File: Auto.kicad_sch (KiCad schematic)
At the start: 25 parts, among them J10 M2, J11 M3, J12 M4, J5 HC-SR04, J9 M1, U4 74HC595, U5 L293DD, U6 L293DD

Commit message: Finalizo el esquematico
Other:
- note added: "OE 0: Habilita enables de drivers y salida de registro de desplazamiento, inhabilita salidas a servos 1: Habilita salidas a servos, inhabilita enables de drivers y salida de registro de desplazamiento"
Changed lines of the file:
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@@
+		)
+	)
+	(text "OE\n0: Habilita enables de drivers y salida de registro de desplazamiento, inhabilita salidas a servos\n1: Habilita salidas a servos, inhabilita enables de drivers y salida de registro de desplazamiento"
+		(exclude_from_sim no)
+		(at 52.832 106.172 0)
+		(effects
+			(font
+				(size 1.27 1.27)
+			)
 		)
 	)

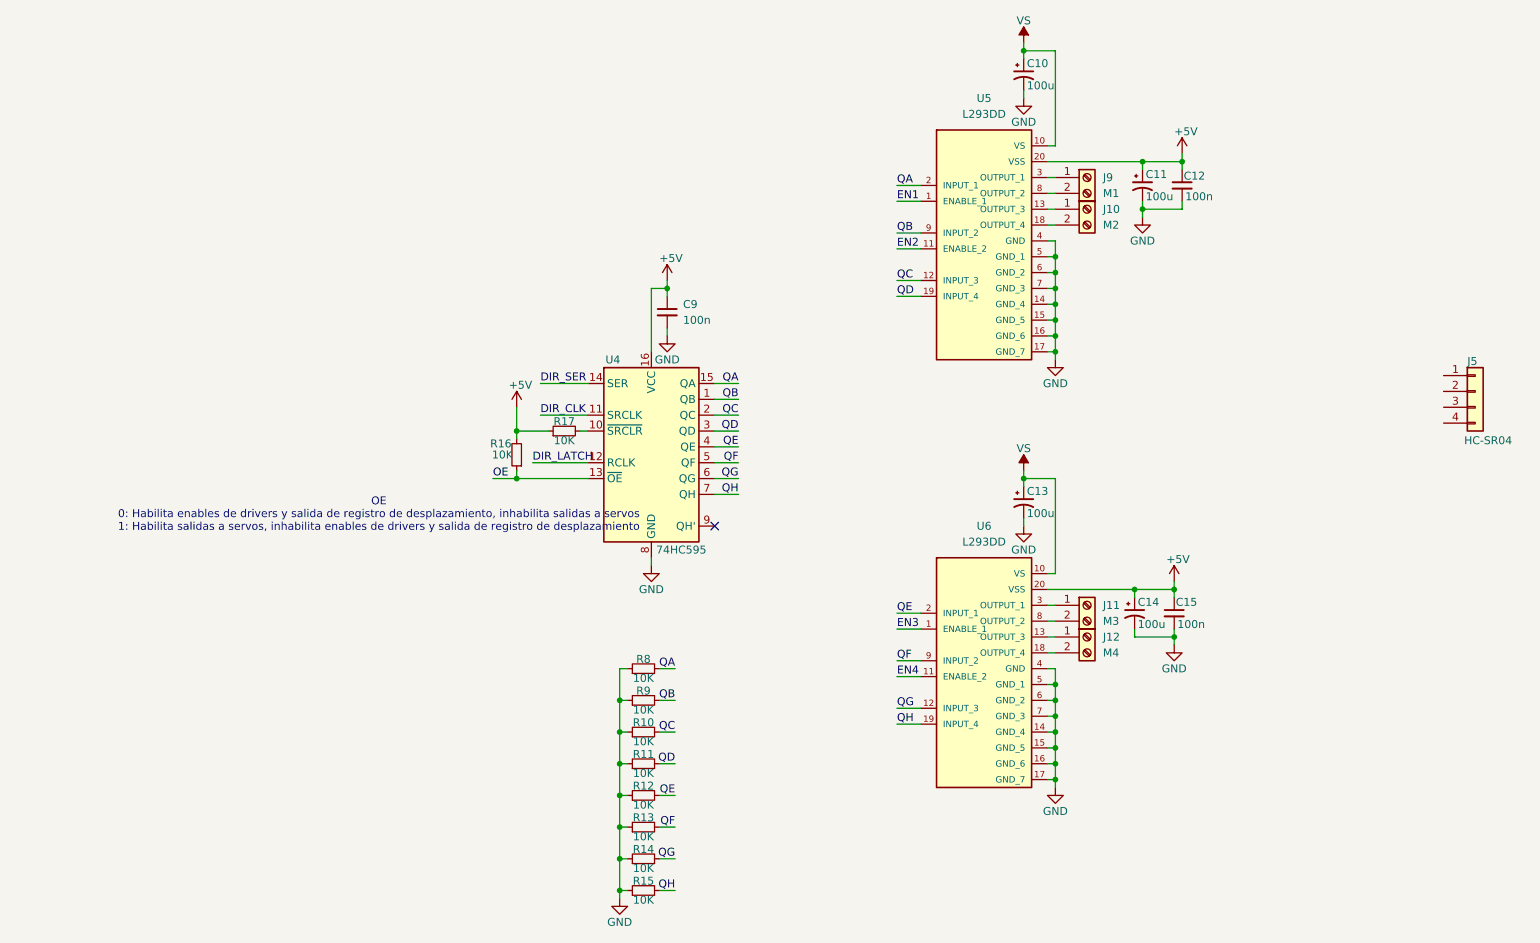
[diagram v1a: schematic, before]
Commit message: Reseteo numeracion de componentes
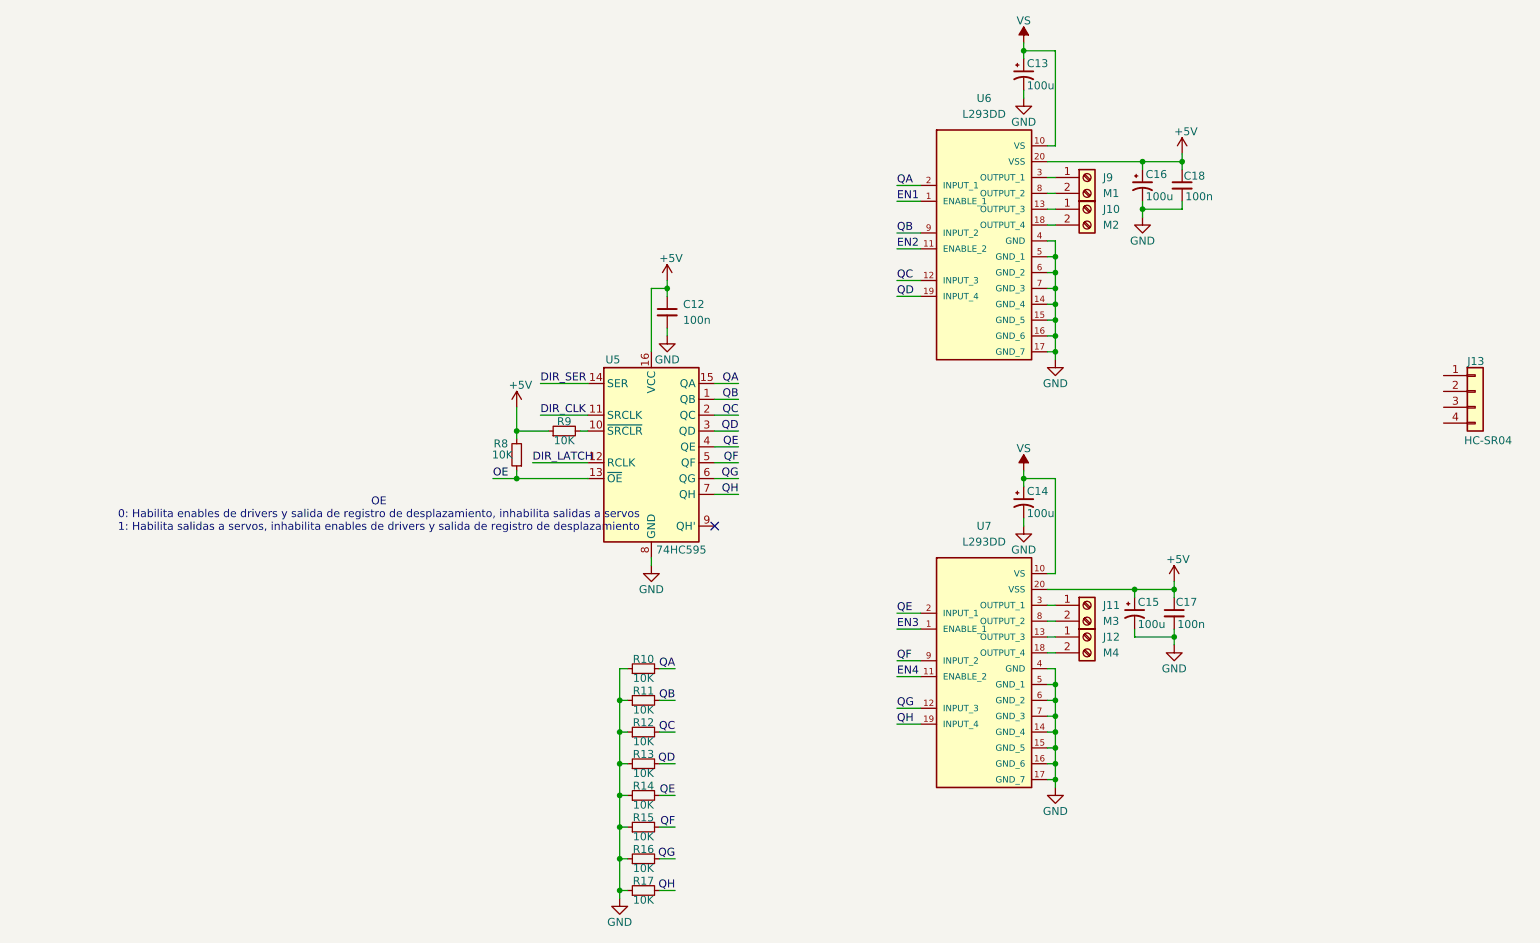
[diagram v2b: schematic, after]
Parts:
- renumbered C9 to C12, C10 to C13, C13 to C14, C14 to C15, C11 to C16, C15 to C17, C12 to C18, J5 to J13, R8 to R10, R9 to R11, R10 to R12, R11 to R13, R12 to R14, R13 to R15, R14 to R16, R15 to R17, R16 to R8, R17 to R9, U4 to U5, U5 to U6, U6 to U7

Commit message: Termino lista de materiales, ubico componentes e inicio ruteo
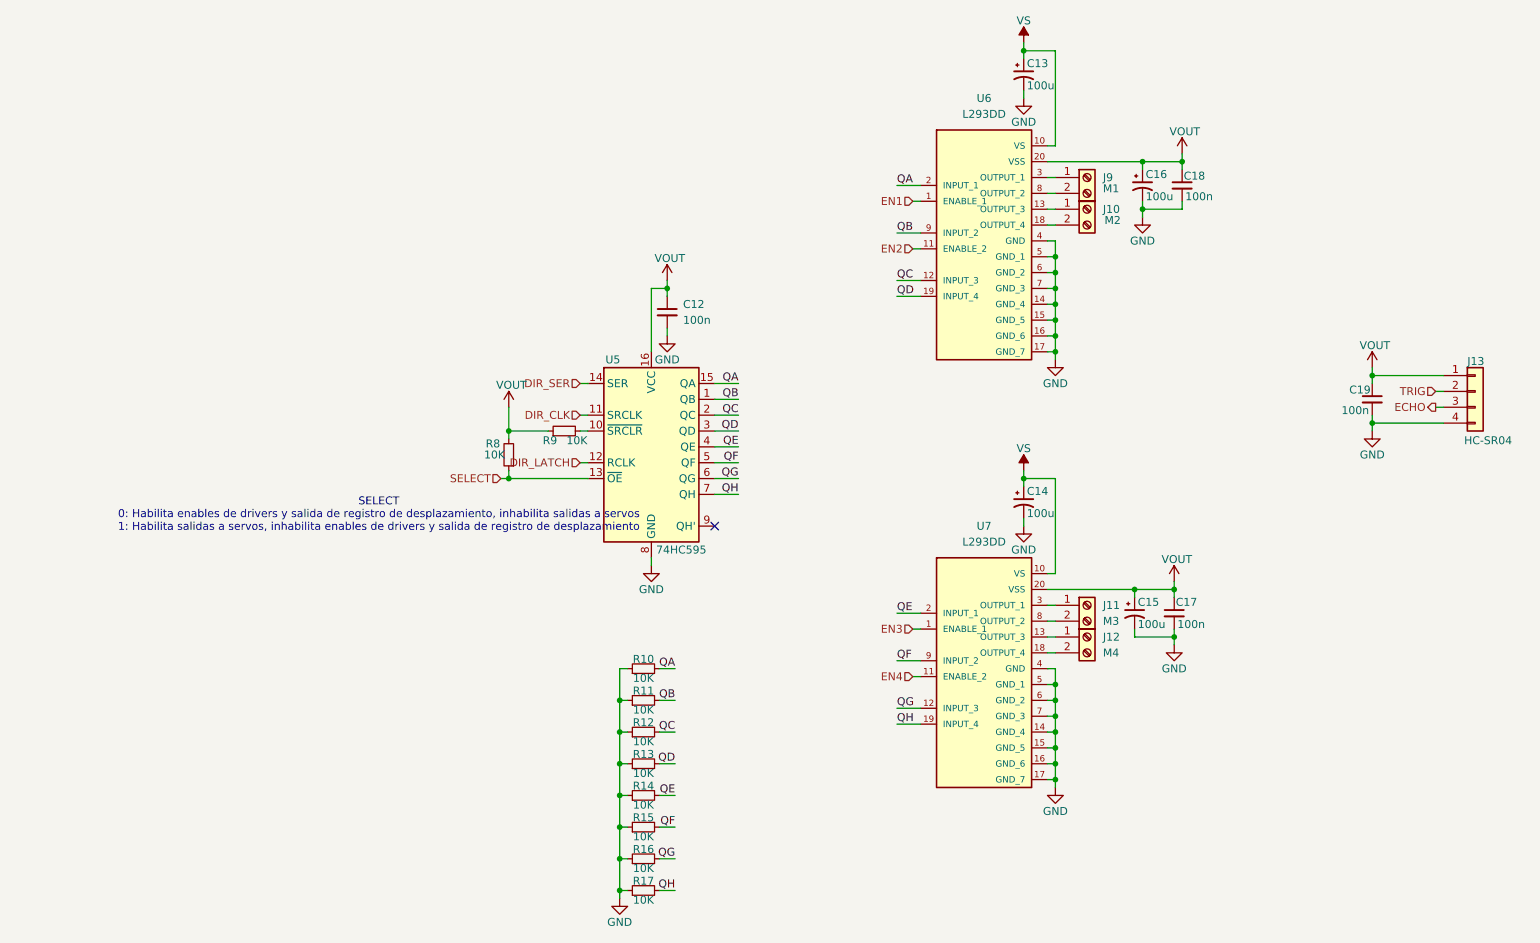
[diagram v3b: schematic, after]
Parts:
- added C19: 100n, Capacitor_SMD:C_0603_1608Metric_Pad1.08x0.95mm_HandSolder, symbol Device:C_Small
- C12, C17, C18: PartNumber (none) -> CL10B104KB8NNNC; PurchaseLink (none) -> https://www.digikey.com/short/0f3djmh4
- C13, C14, C15, C16: footprint Newsanlib:CAP_EEEFK1E101XP -> Capacitor_SMD:CP_Elec_6.3x5.9; PartNumber (none) -> A765EB107M1CLAE025; PurchaseLink (none) -> https://www.digikey.com/en/products/detail/kemet/A765EB107M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
- J13: footprint Connector_PinHeader_1.27mm:PinHeader_1x04_P1.27mm_Vertical -> Connector_PinHeader_2.54mm:PinHeader_1x04_P2.54mm_Vertical
- R10, R11, R12, R13, R14, R15, R16, R17, R8, R9: PartNumber (none) -> RC0603FR-0710KL; PurchaseLink (none) -> https://www.digikey.com/en/products/detail/yageo/RC0603FR-0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
- U5: footprint Package_SO:SOIC-16W_5.3x10.2mm_P1.27mm -> Package_SO:TSSOP-16_4.4x5mm_P0.65mm; PartNumber (none) -> 74HC595PW-Q100,118; PurchaseLink (none) -> https://www.digikey.com/en/products/detail/nexperia-usa-inc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
- U6, U7: PurchaseLink (none) -> https://www.digikey.com/en/products/detail/stmicroelectroni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
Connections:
- net +5V is gone; now on net VOUT: C12.1, C15.1, C16.1, C17.1, C18.1, R8.2, R9.1, U5.16 (VCC), U6.20 (VSS), U7.20 (VSS)
- net GND: now also J13.4 (Pin_4), C19.2
- net VOUT: now reaches J13.1 (Pin_1)
- net VOUT: now also C19.1
- net TRIG: now reaches J13.2 (Pin_2)
- net ECHO: now reaches J13.3 (Pin_3)
- net OE renamed SELECT
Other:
- note added: "SELECT 0: Habilita enables de drivers y salida de registro de desplazamiento, inhabilita salidas a servos 1: Habilita salidas a servos, inhabilita enables de drivers y salida de registro de desplazamiento"
- note removed: "OE 0: Habilita enables de drivers y salida de registro de desplazamiento, inhabilita salidas a servos 1: Habilita salidas a servos, inhabilita enables de drivers y salida de registro de desplazamiento"
- moved on the sheet: R8

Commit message: Agrego capacitores y cambio footprints de borneras
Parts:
- J10, J11, J12, J9: footprint Newsanlib:TerminalBlock_bornier-2_P5.08mm -> TerminalBlock_RND:TerminalBlock_RND_205-00287_1x02_P5.08mm_Horizontal
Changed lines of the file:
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@@
 			)
 		)
-		(property "Footprint" "Newsanlib:TerminalBlock_bornier-2_P5.08mm"
+		(property "Footprint" "TerminalBlock_RND:TerminalBlock_RND_205-00287_1x02_P5.08mm_Horizontal"
 			(at 166.37 120.65 0)
 			(effects
@@
 			)
 		)
-		(property "Footprint" "Newsanlib:TerminalBlock_bornier-2_P5.08mm"
+		(property "Footprint" "TerminalBlock_RND:TerminalBlock_RND_205-00287_1x02_P5.08mm_Horizontal"
 			(at 166.37 52.07 0)
 			(effects
@@
 			)
 		)
-		(property "Footprint" "Newsanlib:TerminalBlock_bornier-2_P5.08mm"
+		(property "Footprint" "TerminalBlock_RND:TerminalBlock_RND_205-00287_1x02_P5.08mm_Horizontal"
 			(at 166.37 125.73 0)
 			(effects
@@
 			)
 		)
-		(property "Footprint" "Newsanlib:TerminalBlock_bornier-2_P5.08mm"
+		(property "Footprint" "TerminalBlock_RND:TerminalBlock_RND_205-00287_1x02_P5.08mm_Horizontal"
 			(at 166.37 57.15 0)
 			(effects

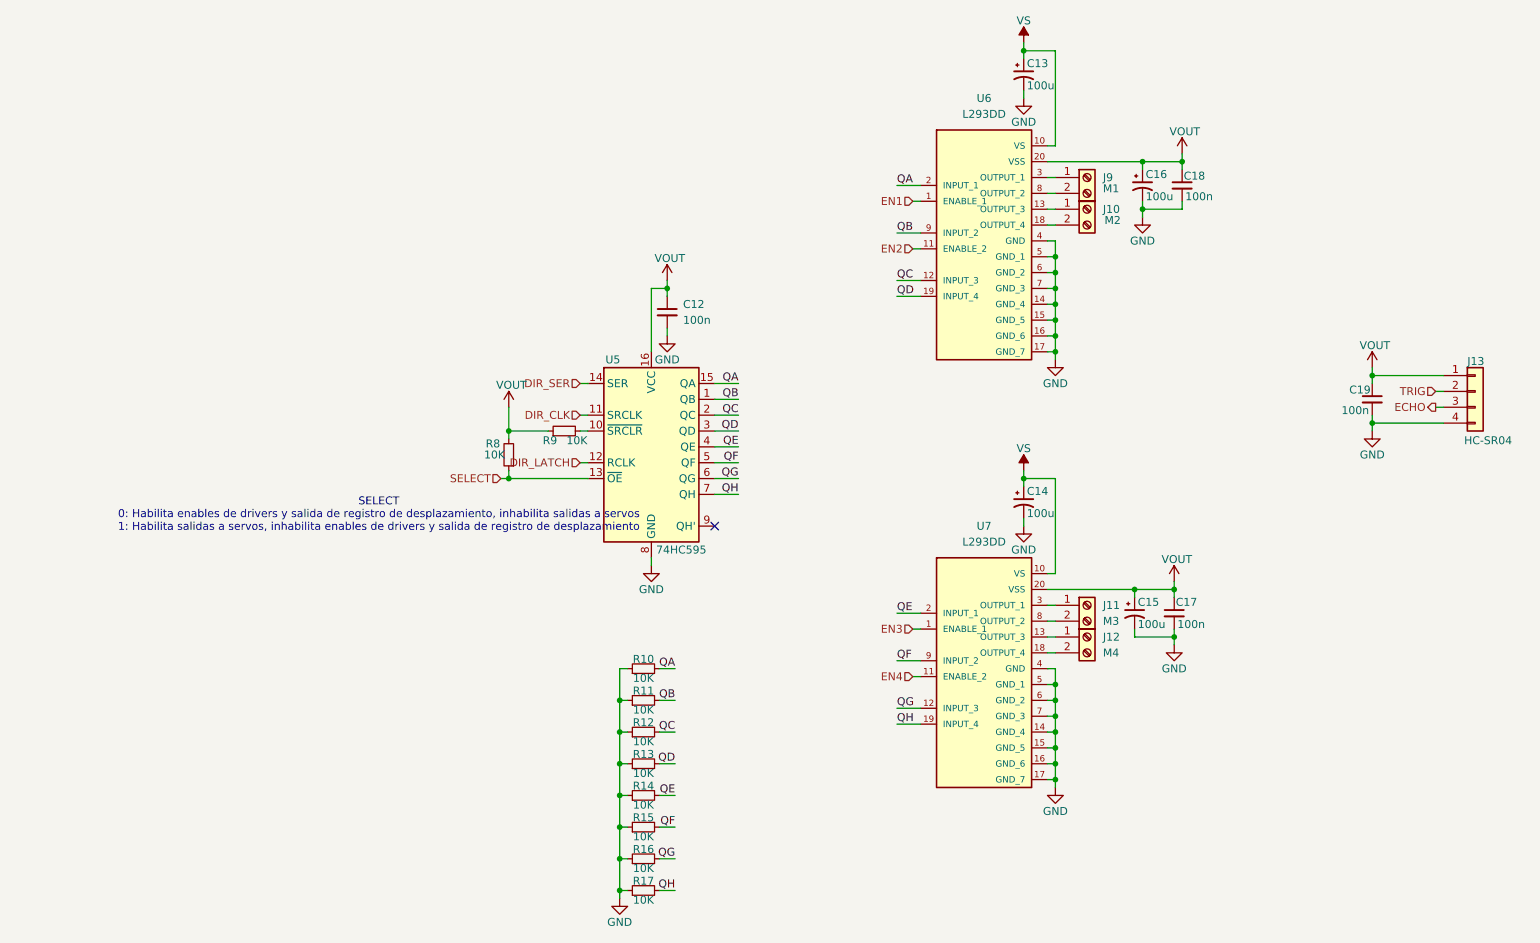
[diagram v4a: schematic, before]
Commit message: Cambio componente principal, hago ubicación en PCB
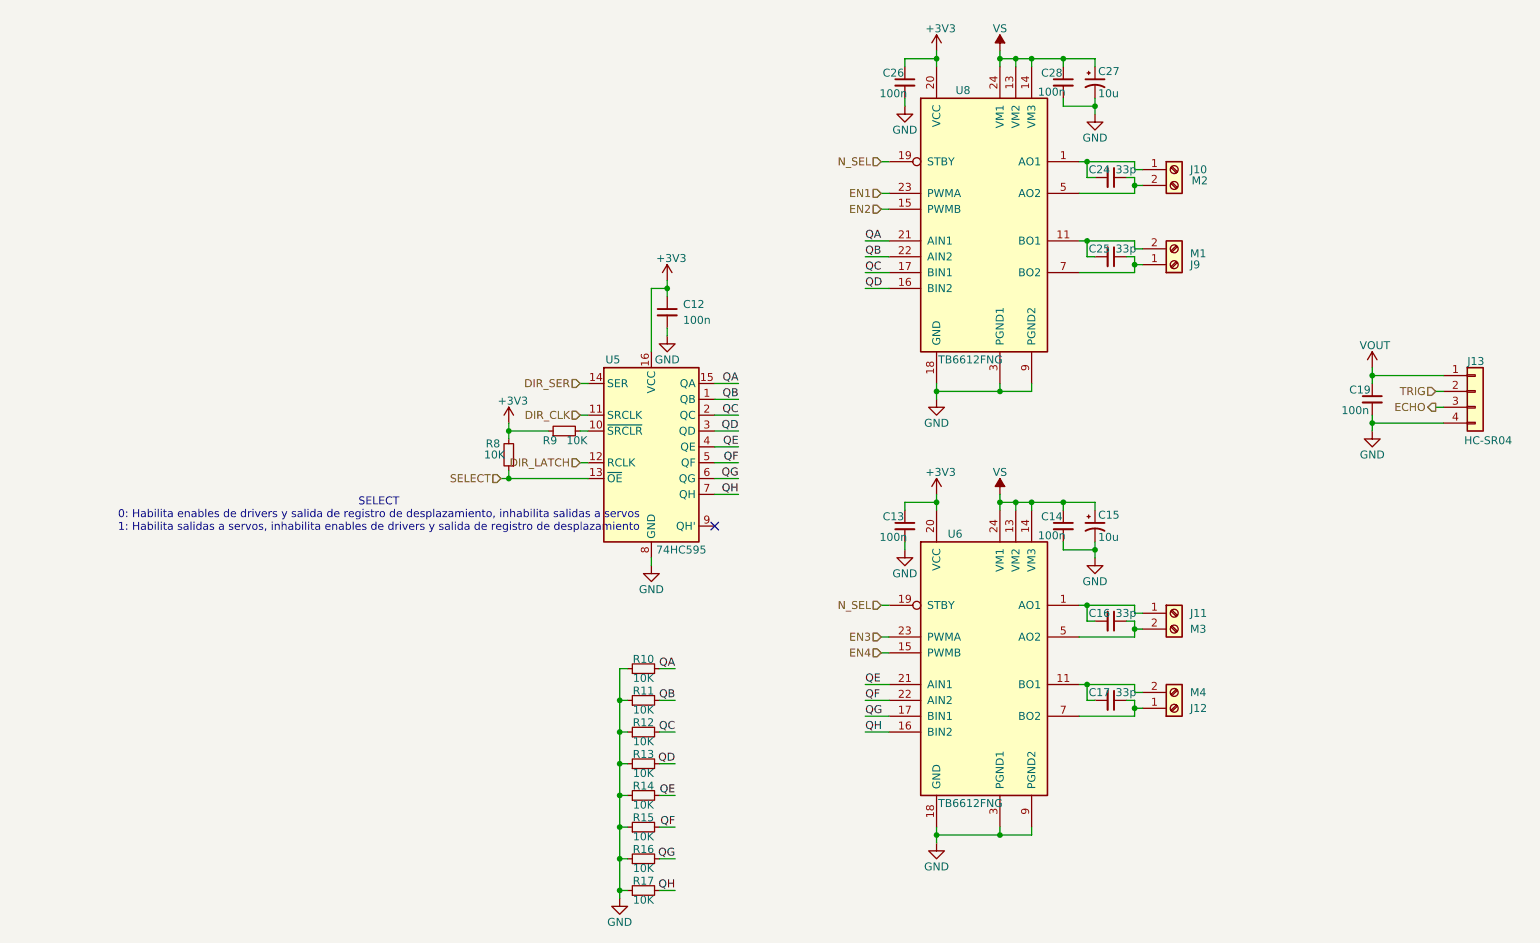
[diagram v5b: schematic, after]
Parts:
- removed C13, C14, C16: 100u, Capacitor_SMD:CP_Elec_6.3x5.9, symbol Device:C_Polarized_Small_US
- removed C18: 100n, Capacitor_SMD:C_0603_1608Metric_Pad1.08x0.95mm_HandSolder, symbol Device:C_Small
- removed U6, U7: L293DD, Newsanlib:SOIC127P1032X265-20N, symbol Newsanlib:L293DD
- added C13, C14, C26, C28: 100n, Capacitor_SMD:C_0603_1608Metric_Pad1.08x0.95mm_HandSolder, symbol Device:C_Small
- added C16, C24, C25: 33p, Capacitor_SMD:C_0402_1005Metric_Pad0.74x0.62mm_HandSolder, symbol Device:C_Small
- added C27: 10u, Capacitor_SMD:CP_Elec_6.3x5.9, symbol Device:C_Polarized_Small_US
- added U6, U8: TB6612FNG, Package_SO:SSOP-24_5.3x8.2mm_P0.65mm, symbol Driver_Motor:TB6612FNG
- C15: value 100u -> 10u; PartNumber A765EB107M1CLAE025 -> 875105544001; PurchaseLink https://www.digikey.com/en/products/detail/kemet/A765EB107M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 -> https://www.digikey.com/en/products/detail/w%C3%BCrth-elekt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
- C17: value 100n -> 33p; footprint Capacitor_SMD:C_0603_1608Metric_Pad1.08x0.95mm_HandSolder -> Capacitor_SMD:C_0402_1005Metric_Pad0.74x0.62mm_HandSolder; PartNumber CL10B104KB8NNNC -> GRM1555C1H330JA01D; PurchaseLink https://www.digikey.com/short/0f3djmh4 -> https://www.digikey.com/en/products/detail/murata-electroni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
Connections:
- net EN1: now also U8.23 (PWMA)
- net EN2: now also U8.15 (PWMB)
- net EN3: now also U6.23 (PWMA)
- net EN4: now also U6.15 (PWMB)
- net GND: now also C13.2, C14.2, C26.2, C27.2, C28.2, U6.10 (PGND2), U6.18 (GND), U6.3 (PGND1), U6.4 (PGND1), U6.9 (PGND2), U8.10 (PGND2), U8.18 (GND), U8.3 (PGND1), U8.4 (PGND1), U8.9 (PGND2); no longer C17.2
- net QA: now also U8.21 (AIN1)
- net QB: now also U8.22 (AIN2)
- net QC: now also U8.17 (BIN1)
- net QD: now also U8.16 (BIN2)
- net QE: now also U6.21 (AIN1)
- net QF: now also U6.22 (AIN2)
- net QG: now also U6.17 (BIN1)
- net QH: now also U6.16 (BIN2)
- net VOUT: no longer C12.1, C15.1, C17.1, R8.2, R9.1, U5.16 (VCC)
- net VS: now also C15.1, C14.1, C27.1, C28.1, U6.13 (VM2), U6.14 (VM3), U6.24 (VM1), U8.13 (VM2), U8.14 (VM3), U8.24 (VM1)
- net at J11.1 (Pin_1): now also C16.2, U6.1 (AO1), U6.2 (AO1)
- net at J11.2 (Pin_2): now also C16.1, U6.5 (AO2), U6.6 (AO2)
- net at J12.1 (Pin_1): now also C17.1, U6.7 (BO2), U6.8 (BO2)
- net at J12.2 (Pin_2): now also C17.2, U6.11 (BO1), U6.12 (BO1)
- net at J9.1 (Pin_1): now also C25.1, U8.7 (BO2), U8.8 (BO2)
- net at J9.2 (Pin_2): now also C25.2, U8.11 (BO1), U8.12 (BO1)
- net at J10.1 (Pin_1): now also C24.2, U8.1 (AO1), U8.2 (AO1)
- net at J10.2 (Pin_2): now also C24.1, U8.5 (AO2), U8.6 (AO2)
- new net +3V3: C12.1, C13.1, C26.1, R8.2, R9.1, U5.16 (VCC), U6.20 (VCC), U8.20 (VCC)
- new net N_SEL: U6.19 (STBY), U8.19 (STBY)
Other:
- moved on the sheet: J10, J11, J12, J9
